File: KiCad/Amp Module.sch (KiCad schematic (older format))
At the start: 50 parts, among them J1 DSP, J2 LITEMOD, U1 NE5532, U2 NE5532, U3 TL072, U4 LM393, U5 74HC08, U6 TL072, U7 AMS1117-5.0

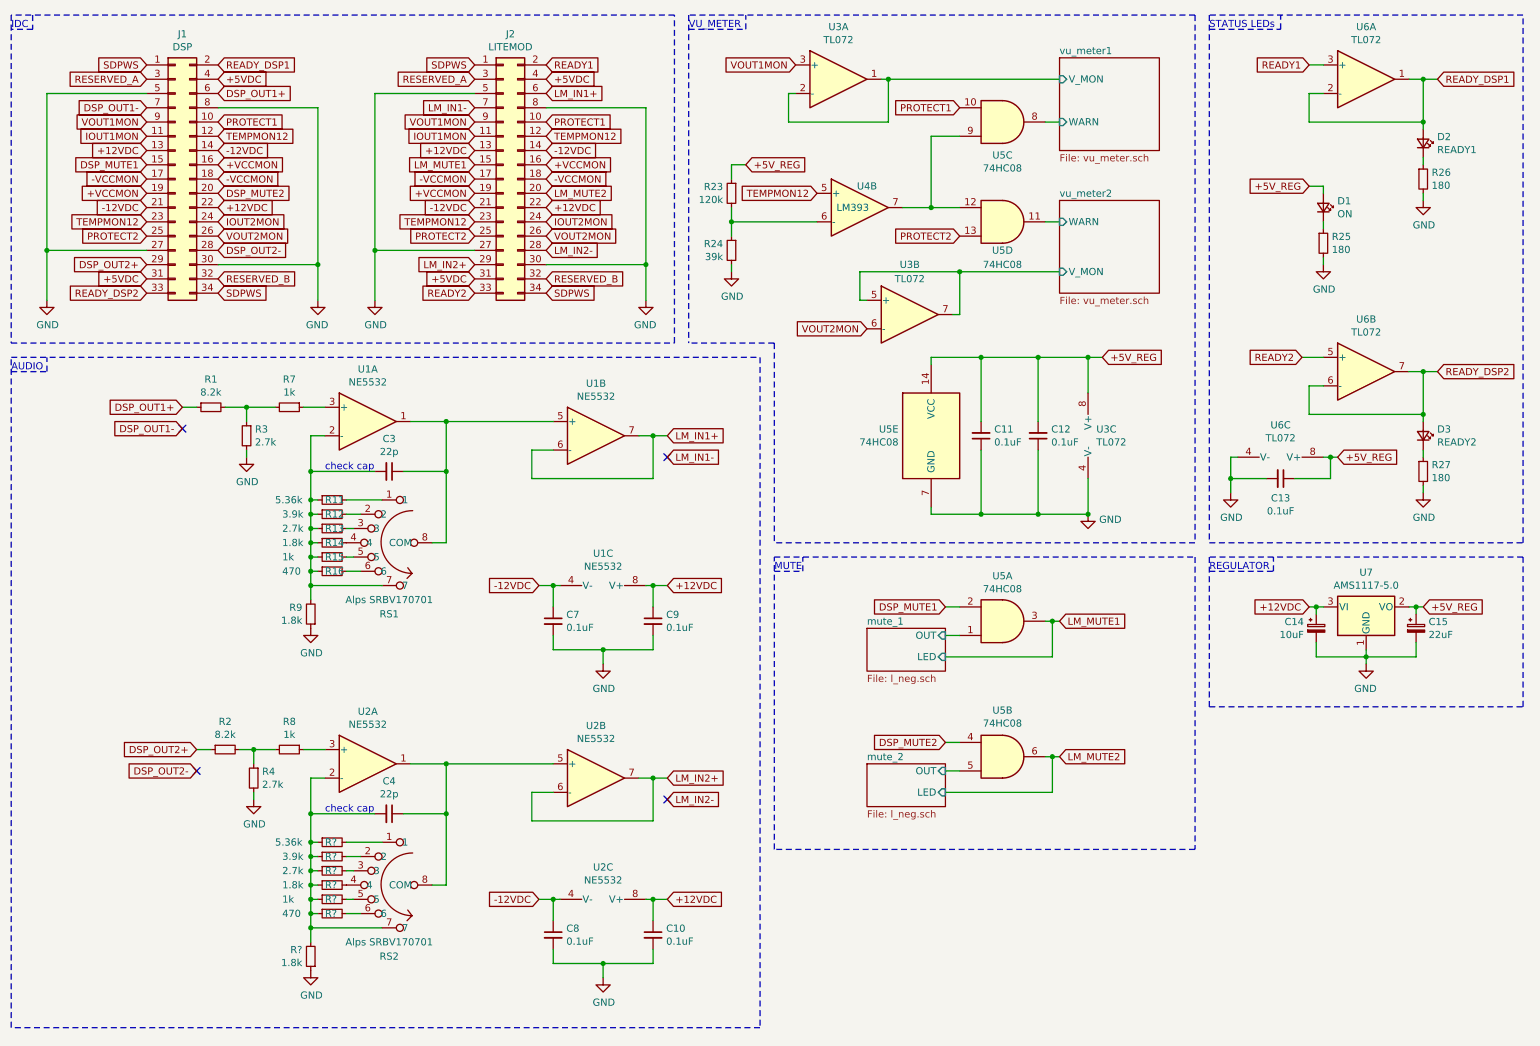
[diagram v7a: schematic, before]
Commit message: finished PCB with TL12
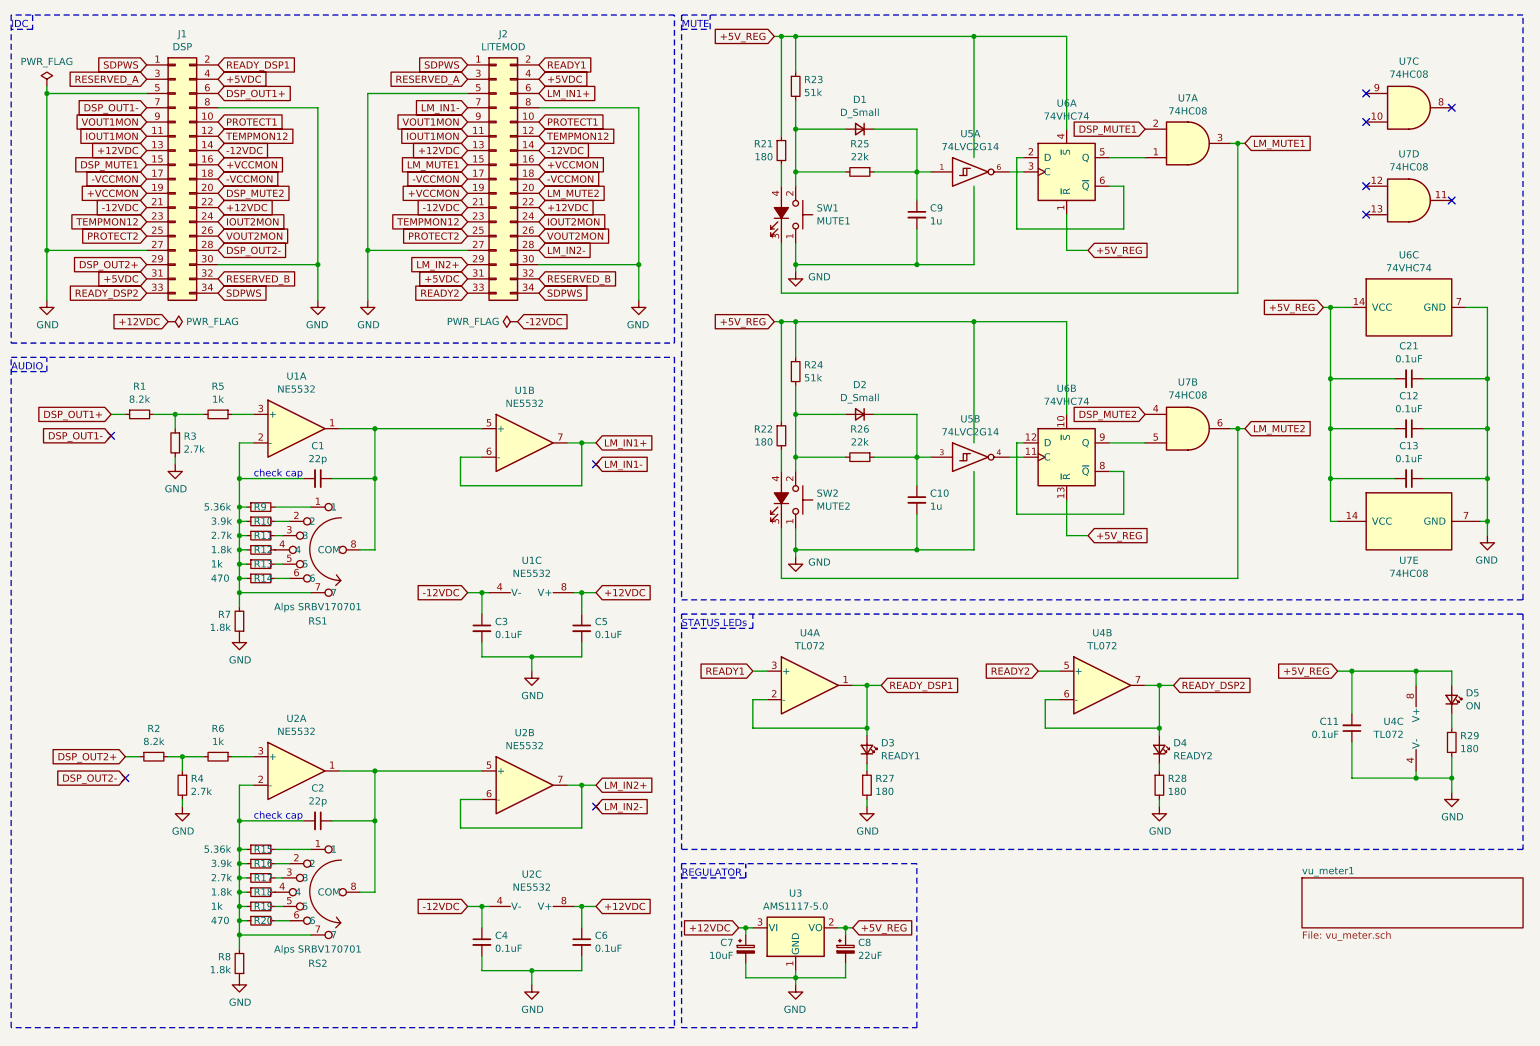
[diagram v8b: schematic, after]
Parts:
- removed C11: 0.1uF, symbol Device:C_Small
- removed U3: TL072, symbol Amplifier_Operational:TL072
- removed U4: LM393, symbol Amp-Module-rescue:LM393-Comparator-Amp-Module-rescue
- removed unit 2 of U5
- removed unit 3 of U5
- removed unit 4 of U5
- removed unit 5 of U5
- added C10, C9: 1u, Capacitor_SMD:C_0805_2012Metric, symbol Device:C_Small
- added C13, C21: 0.1uF, Capacitor_SMD:C_0805_2012Metric, symbol Device:C_Small
- added D1, D2: D_Small, Diode_SMD:D_MiniMELF, symbol Device:D_Small
- added R21, R22: 180, Resistor_SMD:R_0805_2012Metric, symbol Device:R_Small
- added R25, R26: 22k, Resistor_SMD:R_0805_2012Metric, symbol Device:R_Small
- added SW1: MUTE1, AmpModule:Button, symbol Switch:SW_Push_LED
- added SW2: MUTE2, AmpModule:Button, symbol Switch:SW_Push_LED
- added U5: 74LVC2G14, Package_TO_SOT_SMD:SOT-23-6, symbol 74xGxx:74LVC2G14
- added U6: 74VHC74, Package_SO:TSSOP-14_4.4x5mm_P0.65mm, symbol 74xx:74HC74
- added unit 2 of U7
- added unit 3 of U7
- added unit 4 of U7
- added unit 5 of U7
- C1: renamed from C3; footprint (none) -> Capacitor_SMD:C_0805_2012Metric
- C11: renamed from C13; footprint (none) -> Capacitor_SMD:C_0805_2012Metric
- C12: footprint (none) -> Capacitor_SMD:C_0805_2012Metric
- C2: renamed from C4; footprint (none) -> Capacitor_SMD:C_0805_2012Metric
- C3: renamed from C7; footprint (none) -> Capacitor_SMD:C_0805_2012Metric
- C4: renamed from C8; footprint (none) -> Capacitor_SMD:C_0805_2012Metric
- C5: renamed from C9; footprint (none) -> Capacitor_SMD:C_0805_2012Metric
- C6: renamed from C10; footprint (none) -> Capacitor_SMD:C_0805_2012Metric
- C7: renamed from C14; footprint (none) -> Capacitor_SMD:CP_Elec_4x5.3
- C8: renamed from C15; footprint (none) -> Capacitor_SMD:CP_Elec_4x5.3
- D3: renamed from D2; footprint (none) -> LED_THT:LED_Rectangular_W5.0mm_H5.0mm
- D4: renamed from D3; footprint (none) -> LED_THT:LED_Rectangular_W5.0mm_H5.0mm
- D5: renamed from D1; footprint (none) -> LED_THT:LED_Rectangular_W5.0mm_H5.0mm
- J1, J2: footprint (none) -> Connector_IDC:IDC-Header_2x17_P2.54mm_Vertical
- R1, R2, R3, R4: footprint (none) -> Resistor_SMD:R_0805_2012Metric
- R10: renamed from R12; footprint (none) -> Resistor_SMD:R_0805_2012Metric
- R11: renamed from R13; footprint (none) -> Resistor_SMD:R_0805_2012Metric
- R12: renamed from R14; footprint (none) -> Resistor_SMD:R_0805_2012Metric
- R13: renamed from R15; footprint (none) -> Resistor_SMD:R_0805_2012Metric
- R14: renamed from R16; footprint (none) -> Resistor_SMD:R_0805_2012Metric
- R15, R16, R17, R18, R19, R20, R8: renamed from R?; footprint (none) -> Resistor_SMD:R_0805_2012Metric
- R23: value 120k -> 51k; footprint (none) -> Resistor_SMD:R_0805_2012Metric
- R24: value 39k -> 51k; footprint (none) -> Resistor_SMD:R_0805_2012Metric
- R27: renamed from R26; footprint (none) -> Resistor_SMD:R_0805_2012Metric
- R28: renamed from R27; footprint (none) -> Resistor_SMD:R_0805_2012Metric
- R29: renamed from R25; footprint (none) -> Resistor_SMD:R_0805_2012Metric
- R5: renamed from R7; footprint (none) -> Resistor_SMD:R_0805_2012Metric
- R6: renamed from R8; footprint (none) -> Resistor_SMD:R_0805_2012Metric
- R7: renamed from R9; footprint (none) -> Resistor_SMD:R_0805_2012Metric
- R9: renamed from R11; footprint (none) -> Resistor_SMD:R_0805_2012Metric
- RS1, RS2: footprint (none) -> AmpModule:Alps_SRBV170701
- U1, U2: footprint (none) -> Package_SO:SOIC-8_3.9x4.9mm_P1.27mm
- U4: renamed from U6; footprint (none) -> Package_SO:SOIC-8_3.9x4.9mm_P1.27mm
- U7: renamed from U5; footprint (none) -> Package_SO:SOIC-14_3.9x8.7mm_P1.27mm
- renumbered U7 to U3
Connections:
- net DSP_MUTE2: now also U7.4
- net GND: now also C11.1, C10.2, C13.1, C21.1, C9.2, SW1.1, SW2.1, U5.2 (GND), U5.2 (GND), U6.7 (GND), U7.7 (GND); no longer C11.2, R24.2
- net LM_MUTE1: now also SW1.3 (K)
- net LM_MUTE2: now also SW2.3 (K), U7.6
- net at R23.2: now also D1.2 (A), R25.2, SW1.2; no longer R24.1
- net +5V_REG renamed VCC
- net VCC: now also C11.2, R24.1, C13.2, C21.2, R21.1, R22.1, U5.5 (VCC), U5.5 (VCC), U6.1 (~R), U6.10 (~S), U6.13 (~R), U6.14 (VCC), U6.4 (~S), U7.14 (VCC); no longer C11.1
- net mute_1/OUT: no longer names the net of U7.1
- net mute_1/OUT: now also U6.5 (Q)
- new net: R21.2, SW1.4 (A)
- new net: C9.1, D1.1 (K), R25.1, U5.1
- new net: U5.6, U6.3 (C)
- new net: C10.1, D2.1 (K), R26.1, U5.3
- new net: U5.4, U6.11 (C)
- new net: D2.2 (A), R24.2, R26.2, SW2.2
- new net: R22.2, SW2.4 (A)
- new net: U6.9 (Q), U7.5
- new net: U6.2 (D), U6.6 (~Q)
- new net: U6.12 (D), U6.8 (~Q)
- no-connect marks 4 -> 10
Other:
- note removed: "VU_METER"
- moved on the sheet: C1, C11, C2, C3, C4, C5, C6, C7, C8, D3, D4, D5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
